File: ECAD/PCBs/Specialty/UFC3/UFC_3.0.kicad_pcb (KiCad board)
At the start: 2 copper layers, 101.6 x 53.3 mm, 13 parts, among them P1 Digital, P10 CONN_01X01, P11 CONN_01X01, P12 CONN_01X01, P13 CONN_01X01, P2 Power, P3 Analog, P4 Analog, P5 PWM, P6 PWM, P7 Communication, P8 CONN_01X01, P9 CONN_01X01

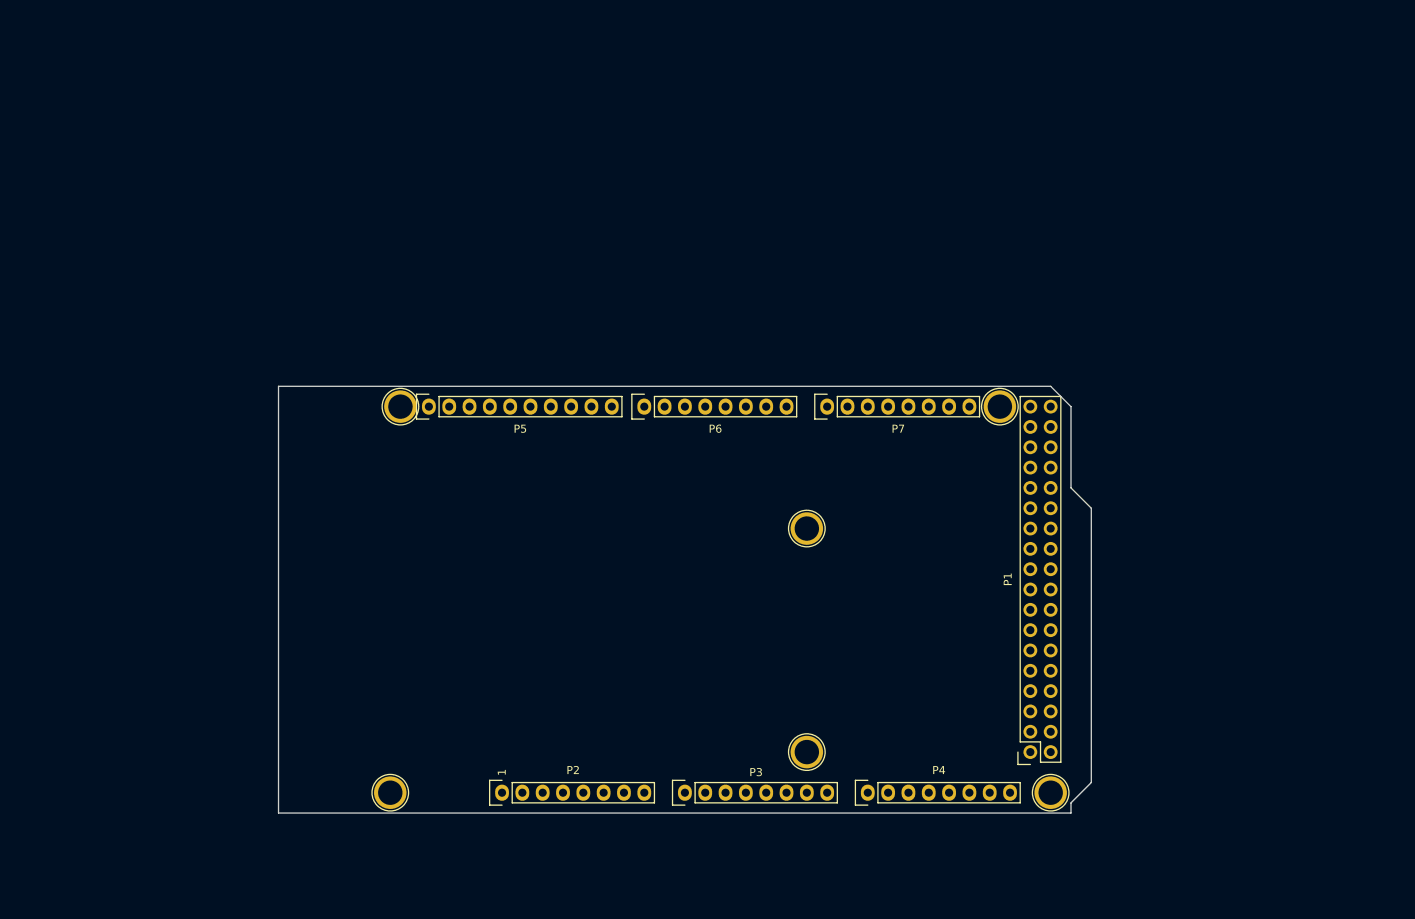
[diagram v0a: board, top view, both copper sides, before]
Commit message: temporary commit, this commit contains a partial version of the routing for UFC v3. along this commit I have added a python script to place the components based on the location listed on a csv file
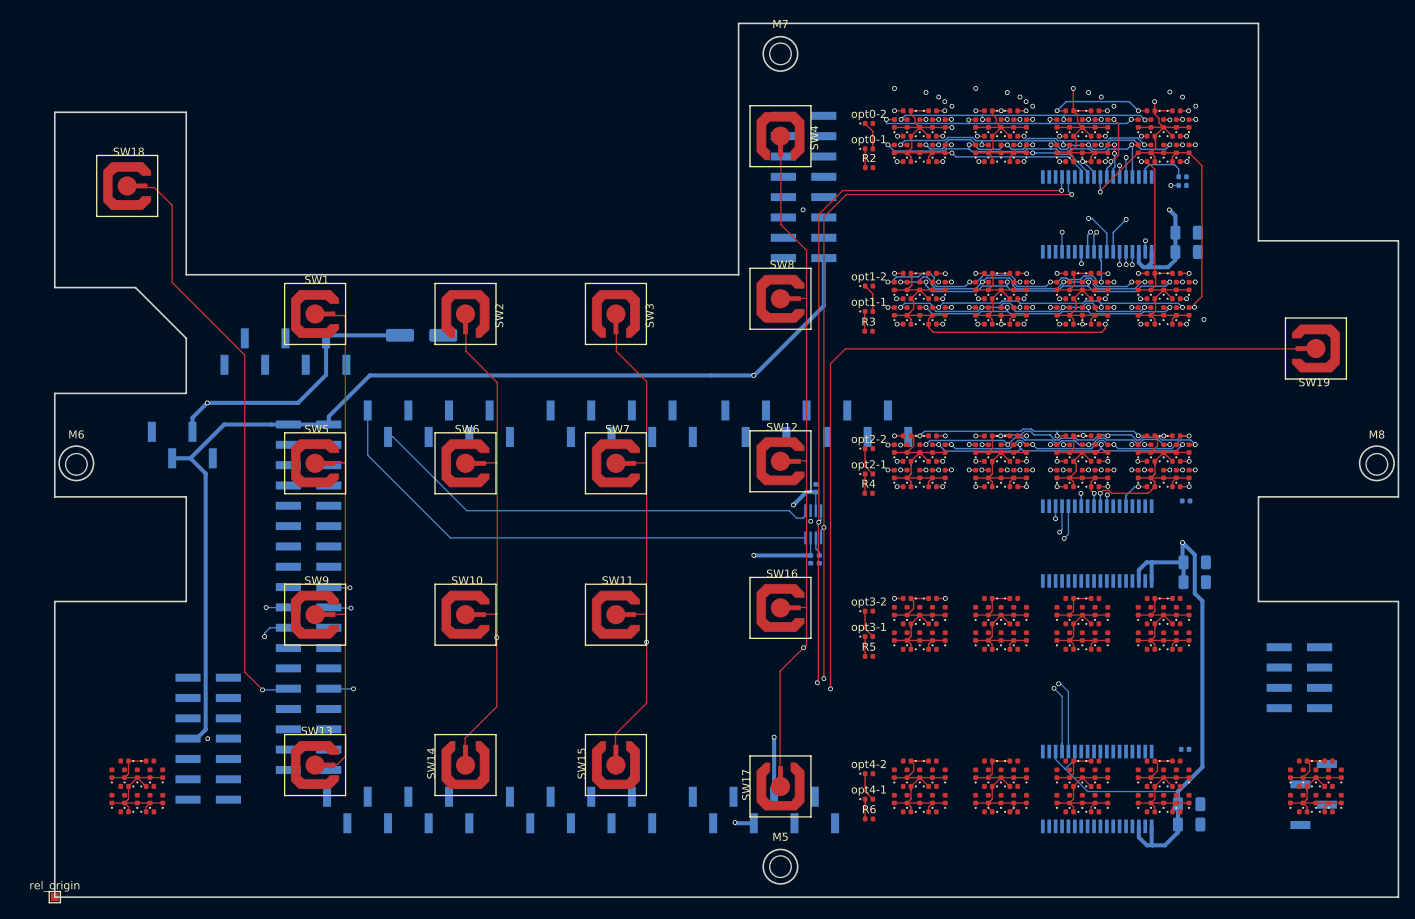
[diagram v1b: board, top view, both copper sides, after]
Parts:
- removed P1: Digital, Socket_Arduino_Mega:Socket_Strip_Arduino_2x18
- removed P2: Power, Socket_Arduino_Mega:Socket_Strip_Arduino_1x08
- removed P3, P4: Analog, Socket_Arduino_Mega:Socket_Strip_Arduino_1x08
- removed P5: PWM, Socket_Arduino_Mega:Socket_Strip_Arduino_1x10
- removed P6: PWM, Socket_Arduino_Mega:Socket_Strip_Arduino_1x08
- added C1: 47uF, Capacitor_SMD:C_1206_3216Metric, B.Cu at (216.9, 49.1)
- added C10: 100uF, Capacitor_SMD:C_1206_3216Metric, B.Cu at (217.2, 120.6)
- added C2: 100uF, Capacitor_SMD:C_1206_3216Metric, B.Cu at (216.9, 51.5)
- added C3: 22pF, Capacitor_SMD:C_0402_1005Metric, B.Cu at (216.4, 43.2)
- added C4: 1uF, Capacitor_SMD:C_0402_1005Metric, B.Cu at (170.5, 81.1)
- added C5: 1uF, Capacitor_SMD:C_0402_1005Metric, B.Cu at (169.9, 90.0)
- added C6: 47uF, Capacitor_SMD:C_1206_3216Metric, B.Cu at (217.9, 90.3)
- added C7: 100uF, Capacitor_SMD:C_1206_3216Metric, B.Cu at (217.9, 92.8)
- added C8: 220uF, Capacitor_SMD:CP_Elec_6.3x7.7, B.Cu at (121.3, 62.0)
- added C9: 47uF, Capacitor_SMD:C_1206_3216Metric, B.Cu at (217.2, 123.1)
- added D1: a, LED_SMD:LED_0402_1005Metric, F.Cu at (181.9, 33.9)
- added D10: g2, LED_SMD:LED_0402_1005Metric, F.Cu at (185.1, 37.1)
- added D100: c, LED_SMD:LED_0402_1005Metric, F.Cu at (217.2, 38.6)
- added D101: d1, LED_SMD:LED_0402_1005Metric, F.Cu at (215.6, 40.2)
- added D102: d2, LED_SMD:LED_0402_1005Metric, F.Cu at (212.4, 40.2)
- added D103: e, LED_SMD:LED_0402_1005Metric, F.Cu at (210.8, 38.6)
- added D104: f, LED_SMD:LED_0402_1005Metric, F.Cu at (210.8, 35.5)
- added D105: g1, LED_SMD:LED_0402_1005Metric, F.Cu at (212.4, 37.1)
- added D106: g2, LED_SMD:LED_0402_1005Metric, F.Cu at (215.6, 37.1)
- added D107: h, LED_SMD:LED_0402_1005Metric, F.Cu at (212.4, 35.5)
- added D108: i, LED_SMD:LED_0402_1005Metric, F.Cu at (214.0, 35.5)
- added D109: j, LED_SMD:LED_0402_1005Metric, F.Cu at (215.6, 35.5)
- added D11: h, LED_SMD:LED_0402_1005Metric, F.Cu at (181.9, 35.5)
- added D110: k, LED_SMD:LED_0402_1005Metric, F.Cu at (215.6, 38.6)
- added D111: L, LED_SMD:LED_0402_1005Metric, F.Cu at (214.0, 38.6)
- added D112: m, LED_SMD:LED_0402_1005Metric, F.Cu at (212.4, 38.6)
- added D113: a, LED_SMD:LED_0402_1005Metric, F.Cu at (212.4, 54.2)
- added D114: a2, LED_SMD:LED_0402_1005Metric, F.Cu at (215.6, 54.2)
- added D115: b, LED_SMD:LED_0402_1005Metric, F.Cu at (217.2, 55.8)
- added D116: c, LED_SMD:LED_0402_1005Metric, F.Cu at (217.2, 59.0)
- added D117: d1, LED_SMD:LED_0402_1005Metric, F.Cu at (215.6, 60.6)
- added D118: d2, LED_SMD:LED_0402_1005Metric, F.Cu at (212.4, 60.6)
- added D119: e, LED_SMD:LED_0402_1005Metric, F.Cu at (210.8, 59.0)
- added D12: i, LED_SMD:LED_0402_1005Metric, F.Cu at (183.5, 35.5)
- added D120: f, LED_SMD:LED_0402_1005Metric, F.Cu at (210.8, 55.8)
- added D121: g1, LED_SMD:LED_0402_1005Metric, F.Cu at (212.4, 57.4)
- added D122: g2, LED_SMD:LED_0402_1005Metric, F.Cu at (215.6, 57.4)
- added D123: h, LED_SMD:LED_0402_1005Metric, F.Cu at (212.4, 55.8)
- added D124: i, LED_SMD:LED_0402_1005Metric, F.Cu at (214.0, 55.8)
- added D125: j, LED_SMD:LED_0402_1005Metric, F.Cu at (215.6, 55.8)
- added D126: k, LED_SMD:LED_0402_1005Metric, F.Cu at (215.6, 59.0)
- added D127: L, LED_SMD:LED_0402_1005Metric, F.Cu at (214.0, 59.0)
- added D128: m, LED_SMD:LED_0402_1005Metric, F.Cu at (212.4, 59.0)
- added D129: a, LED_SMD:LED_0402_1005Metric, F.Cu at (181.9, 74.5)
- added D13: j, LED_SMD:LED_0402_1005Metric, F.Cu at (185.1, 35.5)
- added D130: a2, LED_SMD:LED_0402_1005Metric, F.Cu at (185.1, 74.5)
- added D131: b, LED_SMD:LED_0402_1005Metric, F.Cu at (186.7, 76.1)
- added D132: c, LED_SMD:LED_0402_1005Metric, F.Cu at (186.7, 79.3)
- added D133: d1, LED_SMD:LED_0402_1005Metric, F.Cu at (185.1, 80.9)
- added D134: d2, LED_SMD:LED_0402_1005Metric, F.Cu at (181.9, 80.9)
- added D135: e, LED_SMD:LED_0402_1005Metric, F.Cu at (180.4, 79.3)
- added D136: f, LED_SMD:LED_0402_1005Metric, F.Cu at (180.4, 76.1)
- added D137: g1, LED_SMD:LED_0402_1005Metric, F.Cu at (181.9, 77.7)
- added D138: g2, LED_SMD:LED_0402_1005Metric, F.Cu at (185.1, 77.7)
- added D139: h, LED_SMD:LED_0402_1005Metric, F.Cu at (181.9, 76.1)
- added D14: k, LED_SMD:LED_0402_1005Metric, F.Cu at (185.1, 38.6)
- added D140: i, LED_SMD:LED_0402_1005Metric, F.Cu at (183.5, 76.1)
- added D141: j, LED_SMD:LED_0402_1005Metric, F.Cu at (185.1, 76.1)
- added D142: k, LED_SMD:LED_0402_1005Metric, F.Cu at (185.1, 79.3)
- added D143: L, LED_SMD:LED_0402_1005Metric, F.Cu at (183.5, 79.3)
- added D144: m, LED_SMD:LED_0402_1005Metric, F.Cu at (181.9, 79.3)
- added D145: a, LED_SMD:LED_0402_1005Metric, F.Cu at (181.9, 94.8)
- added D146: a2, LED_SMD:LED_0402_1005Metric, F.Cu at (185.1, 94.8)
- added D147: b, LED_SMD:LED_0402_1005Metric, F.Cu at (186.7, 96.4)
- added D148: c, LED_SMD:LED_0402_1005Metric, F.Cu at (186.7, 99.6)
- added D149: d1, LED_SMD:LED_0402_1005Metric, F.Cu at (185.1, 101.2)
- added D15: L, LED_SMD:LED_0402_1005Metric, F.Cu at (183.5, 38.6)
- added D150: d2, LED_SMD:LED_0402_1005Metric, F.Cu at (181.9, 101.2)
- added D151: e, LED_SMD:LED_0402_1005Metric, F.Cu at (180.4, 99.6)
- added D152: f, LED_SMD:LED_0402_1005Metric, F.Cu at (180.4, 96.4)
- added D153: g1, LED_SMD:LED_0402_1005Metric, F.Cu at (181.9, 98.0)
- added D154: g2, LED_SMD:LED_0402_1005Metric, F.Cu at (185.1, 98.0)
- added D155: h, LED_SMD:LED_0402_1005Metric, F.Cu at (181.9, 96.4)
- added D156: i, LED_SMD:LED_0402_1005Metric, F.Cu at (183.5, 96.4)
- added D157: j, LED_SMD:LED_0402_1005Metric, F.Cu at (185.1, 96.4)
- added D158: k, LED_SMD:LED_0402_1005Metric, F.Cu at (185.1, 99.6)
- added D159: L, LED_SMD:LED_0402_1005Metric, F.Cu at (183.5, 99.6)
- added D16: m, LED_SMD:LED_0402_1005Metric, F.Cu at (181.9, 38.6)
- added D160: m, LED_SMD:LED_0402_1005Metric, F.Cu at (181.9, 99.6)
- added D161: a, LED_SMD:LED_0402_1005Metric, F.Cu at (192.1, 74.5)
- added D162: a2, LED_SMD:LED_0402_1005Metric, F.Cu at (195.3, 74.5)
- added D163: b, LED_SMD:LED_0402_1005Metric, F.Cu at (196.9, 76.1)
- added D164: c, LED_SMD:LED_0402_1005Metric, F.Cu at (196.9, 79.3)
- added D165: d1, LED_SMD:LED_0402_1005Metric, F.Cu at (195.3, 80.9)
- added D166: d2, LED_SMD:LED_0402_1005Metric, F.Cu at (192.1, 80.9)
- added D167: e, LED_SMD:LED_0402_1005Metric, F.Cu at (190.5, 79.3)
- added D168: f, LED_SMD:LED_0402_1005Metric, F.Cu at (190.5, 76.1)
- added D169: g1, LED_SMD:LED_0402_1005Metric, F.Cu at (192.1, 77.7)
- added D17: a, LED_SMD:LED_0402_1005Metric, F.Cu at (181.9, 54.2)
- added D170: g2, LED_SMD:LED_0402_1005Metric, F.Cu at (195.3, 77.7)
- added D171: h, LED_SMD:LED_0402_1005Metric, F.Cu at (192.1, 76.1)
- added D172: i, LED_SMD:LED_0402_1005Metric, F.Cu at (193.7, 76.1)
- added D173: j, LED_SMD:LED_0402_1005Metric, F.Cu at (195.3, 76.1)
- added D174: k, LED_SMD:LED_0402_1005Metric, F.Cu at (195.3, 79.3)
- added D175: L, LED_SMD:LED_0402_1005Metric, F.Cu at (193.7, 79.3)
- added D176: m, LED_SMD:LED_0402_1005Metric, F.Cu at (192.1, 79.3)
- added D177: a, LED_SMD:LED_0402_1005Metric, F.Cu at (192.1, 94.8)
- added D178: a2, LED_SMD:LED_0402_1005Metric, F.Cu at (195.3, 94.8)
- added D179: b, LED_SMD:LED_0402_1005Metric, F.Cu at (196.9, 96.4)
- added D18: a2, LED_SMD:LED_0402_1005Metric, F.Cu at (185.1, 54.2)
- added D180: c, LED_SMD:LED_0402_1005Metric, F.Cu at (196.9, 99.6)
- added D181: d1, LED_SMD:LED_0402_1005Metric, F.Cu at (195.3, 101.2)
- added D182: d2, LED_SMD:LED_0402_1005Metric, F.Cu at (192.1, 101.2)
- added D183: e, LED_SMD:LED_0402_1005Metric, F.Cu at (190.5, 99.6)
- added D184: f, LED_SMD:LED_0402_1005Metric, F.Cu at (190.5, 96.4)
- added D185: g1, LED_SMD:LED_0402_1005Metric, F.Cu at (192.1, 98.0)
- added D186: g2, LED_SMD:LED_0402_1005Metric, F.Cu at (195.3, 98.0)
- added D187: h, LED_SMD:LED_0402_1005Metric, F.Cu at (192.1, 96.4)
- added D188: i, LED_SMD:LED_0402_1005Metric, F.Cu at (193.7, 96.4)
- added D189: j, LED_SMD:LED_0402_1005Metric, F.Cu at (195.3, 96.4)
- added D19: b, LED_SMD:LED_0402_1005Metric, F.Cu at (186.7, 55.8)
- added D190: k, LED_SMD:LED_0402_1005Metric, F.Cu at (195.3, 99.6)
- added D191: L, LED_SMD:LED_0402_1005Metric, F.Cu at (193.7, 99.6)
- added D192: m, LED_SMD:LED_0402_1005Metric, F.Cu at (192.1, 99.6)
- added D193: a, LED_SMD:LED_0402_1005Metric, F.Cu at (202.3, 74.5)
- added D194: a2, LED_SMD:LED_0402_1005Metric, F.Cu at (205.4, 74.5)
- added D195: b, LED_SMD:LED_0402_1005Metric, F.Cu at (207.0, 76.1)
- added D196: c, LED_SMD:LED_0402_1005Metric, F.Cu at (207.0, 79.3)
- added D197: d1, LED_SMD:LED_0402_1005Metric, F.Cu at (205.4, 80.9)
- added D198: d2, LED_SMD:LED_0402_1005Metric, F.Cu at (202.3, 80.9)
- added D199: e, LED_SMD:LED_0402_1005Metric, F.Cu at (200.7, 79.3)
- added D2: a2, LED_SMD:LED_0402_1005Metric, F.Cu at (185.1, 33.9)
- added D20: c, LED_SMD:LED_0402_1005Metric, F.Cu at (186.7, 59.0)
- added D200: f, LED_SMD:LED_0402_1005Metric, F.Cu at (200.7, 76.1)
- added D201: g1, LED_SMD:LED_0402_1005Metric, F.Cu at (202.3, 77.7)
- added D202: g2, LED_SMD:LED_0402_1005Metric, F.Cu at (205.4, 77.7)
- added D203: h, LED_SMD:LED_0402_1005Metric, F.Cu at (202.3, 76.1)
- added D204: i, LED_SMD:LED_0402_1005Metric, F.Cu at (203.9, 76.1)
- added D205: j, LED_SMD:LED_0402_1005Metric, F.Cu at (205.4, 76.1)
- added D206: k, LED_SMD:LED_0402_1005Metric, F.Cu at (205.4, 79.3)
- added D207: L, LED_SMD:LED_0402_1005Metric, F.Cu at (203.9, 79.3)
- added D208: m, LED_SMD:LED_0402_1005Metric, F.Cu at (202.3, 79.3)
- added D209: a, LED_SMD:LED_0402_1005Metric, F.Cu at (202.3, 94.8)
- added D21: d1, LED_SMD:LED_0402_1005Metric, F.Cu at (185.1, 60.6)
- added D210: a2, LED_SMD:LED_0402_1005Metric, F.Cu at (205.4, 94.8)
- added D211: b, LED_SMD:LED_0402_1005Metric, F.Cu at (207.0, 96.4)
- added D212: c, LED_SMD:LED_0402_1005Metric, F.Cu at (207.0, 99.6)
- added D213: d1, LED_SMD:LED_0402_1005Metric, F.Cu at (205.4, 101.2)
- added D214: d2, LED_SMD:LED_0402_1005Metric, F.Cu at (202.3, 101.2)
- added D215: e, LED_SMD:LED_0402_1005Metric, F.Cu at (200.7, 99.6)
- added D216: f, LED_SMD:LED_0402_1005Metric, F.Cu at (200.7, 96.4)
- added D217: g1, LED_SMD:LED_0402_1005Metric, F.Cu at (202.3, 98.0)
- added D218: g2, LED_SMD:LED_0402_1005Metric, F.Cu at (205.4, 98.0)
- added D219: h, LED_SMD:LED_0402_1005Metric, F.Cu at (202.3, 96.4)
- added D22: d2, LED_SMD:LED_0402_1005Metric, F.Cu at (181.9, 60.6)
- added D220: i, LED_SMD:LED_0402_1005Metric, F.Cu at (203.9, 96.4)
- added D221: j, LED_SMD:LED_0402_1005Metric, F.Cu at (205.4, 96.4)
- added D222: k, LED_SMD:LED_0402_1005Metric, F.Cu at (205.4, 99.6)
- added D223: L, LED_SMD:LED_0402_1005Metric, F.Cu at (203.9, 99.6)
- added D224: m, LED_SMD:LED_0402_1005Metric, F.Cu at (202.3, 99.6)
- added D225: a, LED_SMD:LED_0402_1005Metric, F.Cu at (212.4, 74.5)
- added D226: a2, LED_SMD:LED_0402_1005Metric, F.Cu at (215.6, 74.5)
- added D227: b, LED_SMD:LED_0402_1005Metric, F.Cu at (217.2, 76.1)
- added D228: c, LED_SMD:LED_0402_1005Metric, F.Cu at (217.2, 79.3)
- added D229: d1, LED_SMD:LED_0402_1005Metric, F.Cu at (215.6, 80.9)
- added D23: e, LED_SMD:LED_0402_1005Metric, F.Cu at (180.4, 59.0)
- added D230: d2, LED_SMD:LED_0402_1005Metric, F.Cu at (212.4, 80.9)
- added D231: e, LED_SMD:LED_0402_1005Metric, F.Cu at (210.8, 79.3)
- added D232: f, LED_SMD:LED_0402_1005Metric, F.Cu at (210.8, 76.1)
- added D233: g1, LED_SMD:LED_0402_1005Metric, F.Cu at (212.4, 77.7)
- added D234: g2, LED_SMD:LED_0402_1005Metric, F.Cu at (215.6, 77.7)
- added D235: h, LED_SMD:LED_0402_1005Metric, F.Cu at (212.4, 76.1)
- added D236: i, LED_SMD:LED_0402_1005Metric, F.Cu at (214.0, 76.1)
- added D237: j, LED_SMD:LED_0402_1005Metric, F.Cu at (215.6, 76.1)
- added D238: k, LED_SMD:LED_0402_1005Metric, F.Cu at (215.6, 79.3)
- added D239: L, LED_SMD:LED_0402_1005Metric, F.Cu at (214.0, 79.3)
- added D24: f, LED_SMD:LED_0402_1005Metric, F.Cu at (180.4, 55.8)
- added D240: m, LED_SMD:LED_0402_1005Metric, F.Cu at (212.4, 79.3)
- added D241: a, LED_SMD:LED_0402_1005Metric, F.Cu at (212.4, 94.8)
- added D242: a2, LED_SMD:LED_0402_1005Metric, F.Cu at (215.6, 94.8)
- added D243: b, LED_SMD:LED_0402_1005Metric, F.Cu at (217.2, 96.4)
- added D244: c, LED_SMD:LED_0402_1005Metric, F.Cu at (217.2, 99.6)
- added D245: d1, LED_SMD:LED_0402_1005Metric, F.Cu at (215.6, 101.2)
- added D246: d2, LED_SMD:LED_0402_1005Metric, F.Cu at (212.4, 101.2)
- added D247: e, LED_SMD:LED_0402_1005Metric, F.Cu at (210.8, 99.6)
- added D248: f, LED_SMD:LED_0402_1005Metric, F.Cu at (210.8, 96.4)
- added D249: g1, LED_SMD:LED_0402_1005Metric, F.Cu at (212.4, 98.0)
- added D25: g1, LED_SMD:LED_0402_1005Metric, F.Cu at (181.9, 57.4)
- added D250: g2, LED_SMD:LED_0402_1005Metric, F.Cu at (215.6, 98.0)
- added D251: h, LED_SMD:LED_0402_1005Metric, F.Cu at (212.4, 96.4)
- added D252: i, LED_SMD:LED_0402_1005Metric, F.Cu at (214.0, 96.4)
- added D253: j, LED_SMD:LED_0402_1005Metric, F.Cu at (215.6, 96.4)
- added D254: k, LED_SMD:LED_0402_1005Metric, F.Cu at (215.6, 99.6)
- added D255: L, LED_SMD:LED_0402_1005Metric, F.Cu at (214.0, 99.6)
- added D256: m, LED_SMD:LED_0402_1005Metric, F.Cu at (212.4, 99.6)
- added D257: a, LED_SMD:LED_0402_1005Metric, F.Cu at (181.9, 115.2)
- added D258: a2, LED_SMD:LED_0402_1005Metric, F.Cu at (185.1, 115.2)
- added D259: b, LED_SMD:LED_0402_1005Metric, F.Cu at (186.7, 116.8)
- added D26: g2, LED_SMD:LED_0402_1005Metric, F.Cu at (185.1, 57.4)
- added D260: c, LED_SMD:LED_0402_1005Metric, F.Cu at (186.7, 119.9)
- added D261: d1, LED_SMD:LED_0402_1005Metric, F.Cu at (185.1, 121.5)
- added D262: d2, LED_SMD:LED_0402_1005Metric, F.Cu at (181.9, 121.5)
- added D263: e, LED_SMD:LED_0402_1005Metric, F.Cu at (180.4, 119.9)
- added D264: f, LED_SMD:LED_0402_1005Metric, F.Cu at (180.4, 116.8)
- added D265: g1, LED_SMD:LED_0402_1005Metric, F.Cu at (181.9, 118.3)
- added D266: g2, LED_SMD:LED_0402_1005Metric, F.Cu at (185.1, 118.3)
- added D267: h, LED_SMD:LED_0402_1005Metric, F.Cu at (181.9, 116.8)
- added D268: i, LED_SMD:LED_0402_1005Metric, F.Cu at (183.5, 116.8)
- added D269: j, LED_SMD:LED_0402_1005Metric, F.Cu at (185.1, 116.8)
- added D27: h, LED_SMD:LED_0402_1005Metric, F.Cu at (181.9, 55.8)
- added D270: k, LED_SMD:LED_0402_1005Metric, F.Cu at (185.1, 119.9)
- added D271: L, LED_SMD:LED_0402_1005Metric, F.Cu at (183.5, 119.9)
- added D272: m, LED_SMD:LED_0402_1005Metric, F.Cu at (181.9, 119.9)
- added D273: a, LED_SMD:LED_0402_1005Metric, F.Cu at (84.1, 115.2)
- added D274: a2, LED_SMD:LED_0402_1005Metric, F.Cu at (87.3, 115.2)
- added D275: b, LED_SMD:LED_0402_1005Metric, F.Cu at (88.9, 116.8)
- added D276: c, LED_SMD:LED_0402_1005Metric, F.Cu at (88.9, 119.9)
- added D277: d1, LED_SMD:LED_0402_1005Metric, F.Cu at (87.3, 121.5)
- added D278: d2, LED_SMD:LED_0402_1005Metric, F.Cu at (84.1, 121.5)
- added D279: e, LED_SMD:LED_0402_1005Metric, F.Cu at (82.5, 119.9)
- added D28: i, LED_SMD:LED_0402_1005Metric, F.Cu at (183.5, 55.8)
- added D280: f, LED_SMD:LED_0402_1005Metric, F.Cu at (82.5, 116.8)
- added D281: g1, LED_SMD:LED_0402_1005Metric, F.Cu at (84.1, 118.3)
- added D282: g2, LED_SMD:LED_0402_1005Metric, F.Cu at (87.3, 118.3)
- added D283: h, LED_SMD:LED_0402_1005Metric, F.Cu at (84.1, 116.8)
- added D284: i, LED_SMD:LED_0402_1005Metric, F.Cu at (85.7, 116.8)
- added D285: j, LED_SMD:LED_0402_1005Metric, F.Cu at (87.3, 116.8)
- added D286: k, LED_SMD:LED_0402_1005Metric, F.Cu at (87.3, 119.9)
- added D287: L, LED_SMD:LED_0402_1005Metric, F.Cu at (85.7, 119.9)
- added D288: m, LED_SMD:LED_0402_1005Metric, F.Cu at (84.1, 119.9)
- added D289: a, LED_SMD:LED_0402_1005Metric, F.Cu at (192.1, 115.2)
- added D29: j, LED_SMD:LED_0402_1005Metric, F.Cu at (185.1, 55.8)
- added D290: a2, LED_SMD:LED_0402_1005Metric, F.Cu at (195.3, 115.2)
- added D291: b, LED_SMD:LED_0402_1005Metric, F.Cu at (196.9, 116.8)
- added D292: c, LED_SMD:LED_0402_1005Metric, F.Cu at (196.9, 119.9)
- added D293: d1, LED_SMD:LED_0402_1005Metric, F.Cu at (195.3, 121.5)
- added D294: d2, LED_SMD:LED_0402_1005Metric, F.Cu at (192.1, 121.5)
- added D295: e, LED_SMD:LED_0402_1005Metric, F.Cu at (190.5, 119.9)
- added D296: f, LED_SMD:LED_0402_1005Metric, F.Cu at (190.5, 116.8)
- added D297: g1, LED_SMD:LED_0402_1005Metric, F.Cu at (192.1, 118.3)
- added D298: g2, LED_SMD:LED_0402_1005Metric, F.Cu at (195.3, 118.3)
- added D299: h, LED_SMD:LED_0402_1005Metric, F.Cu at (192.1, 116.8)
- added D3: b, LED_SMD:LED_0402_1005Metric, F.Cu at (186.7, 35.5)
- added D30: k, LED_SMD:LED_0402_1005Metric, F.Cu at (185.1, 59.0)
- added D300: i, LED_SMD:LED_0402_1005Metric, F.Cu at (193.7, 116.8)
- added D301: j, LED_SMD:LED_0402_1005Metric, F.Cu at (195.3, 116.8)
- added D302: k, LED_SMD:LED_0402_1005Metric, F.Cu at (195.3, 119.9)
- added D303: L, LED_SMD:LED_0402_1005Metric, F.Cu at (193.7, 119.9)
- added D304: m, LED_SMD:LED_0402_1005Metric, F.Cu at (192.1, 119.9)
- added D305: a, LED_SMD:LED_0402_1005Metric, F.Cu at (231.5, 115.2)
- added D306: a2, LED_SMD:LED_0402_1005Metric, F.Cu at (234.6, 115.2)
- added D307: b, LED_SMD:LED_0402_1005Metric, F.Cu at (236.2, 116.8)
- added D308: c, LED_SMD:LED_0402_1005Metric, F.Cu at (236.2, 119.9)
- added D309: d1, LED_SMD:LED_0402_1005Metric, F.Cu at (234.6, 121.5)
- added D31: L, LED_SMD:LED_0402_1005Metric, F.Cu at (183.5, 59.0)
- added D310: d2, LED_SMD:LED_0402_1005Metric, F.Cu at (231.5, 121.5)
- added D311: e, LED_SMD:LED_0402_1005Metric, F.Cu at (229.9, 119.9)
- added D312: f, LED_SMD:LED_0402_1005Metric, F.Cu at (229.9, 116.8)
- added D313: g1, LED_SMD:LED_0402_1005Metric, F.Cu at (231.5, 118.3)
- added D314: g2, LED_SMD:LED_0402_1005Metric, F.Cu at (234.6, 118.3)
- added D315: h, LED_SMD:LED_0402_1005Metric, F.Cu at (231.5, 116.8)
- added D316: i, LED_SMD:LED_0402_1005Metric, F.Cu at (233.0, 116.8)
- added D317: j, LED_SMD:LED_0402_1005Metric, F.Cu at (234.6, 116.8)
- added D318: k, LED_SMD:LED_0402_1005Metric, F.Cu at (234.6, 119.9)
- added D319: L, LED_SMD:LED_0402_1005Metric, F.Cu at (233.0, 119.9)
- added D32: m, LED_SMD:LED_0402_1005Metric, F.Cu at (181.9, 59.0)
- added D320: m, LED_SMD:LED_0402_1005Metric, F.Cu at (231.5, 119.9)
- added D321: a, LED_SMD:LED_0402_1005Metric, F.Cu at (202.3, 115.2)
- added D322: a2, LED_SMD:LED_0402_1005Metric, F.Cu at (205.4, 115.2)
- added D323: b, LED_SMD:LED_0402_1005Metric, F.Cu at (207.0, 116.8)
- added D324: c, LED_SMD:LED_0402_1005Metric, F.Cu at (207.0, 119.9)
- added D325: d1, LED_SMD:LED_0402_1005Metric, F.Cu at (205.4, 121.5)
- added D326: d2, LED_SMD:LED_0402_1005Metric, F.Cu at (202.3, 121.5)
- added D327: e, LED_SMD:LED_0402_1005Metric, F.Cu at (200.7, 119.9)
- added D328: f, LED_SMD:LED_0402_1005Metric, F.Cu at (200.7, 116.8)
- added D329: g1, LED_SMD:LED_0402_1005Metric, F.Cu at (202.3, 118.3)
- added D33: a, LED_SMD:LED_0402_1005Metric, F.Cu at (192.1, 33.9)
- added D330: g2, LED_SMD:LED_0402_1005Metric, F.Cu at (205.4, 118.3)
- added D331: h, LED_SMD:LED_0402_1005Metric, F.Cu at (202.3, 116.8)
- added D332: i, LED_SMD:LED_0402_1005Metric, F.Cu at (203.9, 116.8)
- added D333: j, LED_SMD:LED_0402_1005Metric, F.Cu at (205.4, 116.8)
- added D334: k, LED_SMD:LED_0402_1005Metric, F.Cu at (205.4, 119.9)
- added D335: L, LED_SMD:LED_0402_1005Metric, F.Cu at (203.9, 119.9)
- added D336: m, LED_SMD:LED_0402_1005Metric, F.Cu at (202.3, 119.9)
- added D337: a, LED_SMD:LED_0402_1005Metric, F.Cu at (212.4, 115.2)
- added D338: a2, LED_SMD:LED_0402_1005Metric, F.Cu at (215.6, 115.2)
- added D339: b, LED_SMD:LED_0402_1005Metric, F.Cu at (217.2, 116.8)
- added D34: a2, LED_SMD:LED_0402_1005Metric, F.Cu at (195.3, 33.9)
- added D340: c, LED_SMD:LED_0402_1005Metric, F.Cu at (217.2, 119.9)
- added D341: d1, LED_SMD:LED_0402_1005Metric, F.Cu at (215.6, 121.5)
- added D342: d2, LED_SMD:LED_0402_1005Metric, F.Cu at (212.4, 121.5)
- added D343: e, LED_SMD:LED_0402_1005Metric, F.Cu at (210.8, 119.9)
- added D344: f, LED_SMD:LED_0402_1005Metric, F.Cu at (210.8, 116.8)
- added D345: g1, LED_SMD:LED_0402_1005Metric, F.Cu at (212.4, 118.3)
- added D346: g2, LED_SMD:LED_0402_1005Metric, F.Cu at (215.6, 118.3)
- added D347: h, LED_SMD:LED_0402_1005Metric, F.Cu at (212.4, 116.8)
- added D348: i, LED_SMD:LED_0402_1005Metric, F.Cu at (214.0, 116.8)
- added D349: j, LED_SMD:LED_0402_1005Metric, F.Cu at (215.6, 116.8)
- added D35: b, LED_SMD:LED_0402_1005Metric, F.Cu at (196.9, 35.5)
- added D350: k, LED_SMD:LED_0402_1005Metric, F.Cu at (215.6, 119.9)
- added D351: L, LED_SMD:LED_0402_1005Metric, F.Cu at (214.0, 119.9)
- added D352: m, LED_SMD:LED_0402_1005Metric, F.Cu at (212.4, 119.9)
- added D36: c, LED_SMD:LED_0402_1005Metric, F.Cu at (196.9, 38.6)
- added D37: d1, LED_SMD:LED_0402_1005Metric, F.Cu at (195.3, 40.2)
- added D38: d2, LED_SMD:LED_0402_1005Metric, F.Cu at (192.1, 40.2)
- added D39: e, LED_SMD:LED_0402_1005Metric, F.Cu at (190.5, 38.6)
- added D4: c, LED_SMD:LED_0402_1005Metric, F.Cu at (186.7, 38.6)
- added D40: f, LED_SMD:LED_0402_1005Metric, F.Cu at (190.5, 35.5)
- added D41: g1, LED_SMD:LED_0402_1005Metric, F.Cu at (192.1, 37.1)
- added D42: g2, LED_SMD:LED_0402_1005Metric, F.Cu at (195.3, 37.1)
- added D43: h, LED_SMD:LED_0402_1005Metric, F.Cu at (192.1, 35.5)
- added D44: i, LED_SMD:LED_0402_1005Metric, F.Cu at (193.7, 35.5)
- added D45: j, LED_SMD:LED_0402_1005Metric, F.Cu at (195.3, 35.5)
- added D46: k, LED_SMD:LED_0402_1005Metric, F.Cu at (195.3, 38.6)
- added D47: L, LED_SMD:LED_0402_1005Metric, F.Cu at (193.7, 38.6)
- added D48: m, LED_SMD:LED_0402_1005Metric, F.Cu at (192.1, 38.6)
- added D49: a, LED_SMD:LED_0402_1005Metric, F.Cu at (192.1, 54.2)
- added D5: d1, LED_SMD:LED_0402_1005Metric, F.Cu at (185.1, 40.2)
- added D50: a2, LED_SMD:LED_0402_1005Metric, F.Cu at (195.3, 54.2)
- added D51: b, LED_SMD:LED_0402_1005Metric, F.Cu at (196.9, 55.8)
- added D52: c, LED_SMD:LED_0402_1005Metric, F.Cu at (196.9, 59.0)
- added D53: d1, LED_SMD:LED_0402_1005Metric, F.Cu at (195.3, 60.6)
- added D54: d2, LED_SMD:LED_0402_1005Metric, F.Cu at (192.1, 60.6)
- added D55: e, LED_SMD:LED_0402_1005Metric, F.Cu at (190.5, 59.0)
- added D56: f, LED_SMD:LED_0402_1005Metric, F.Cu at (190.5, 55.8)
- added D57: g1, LED_SMD:LED_0402_1005Metric, F.Cu at (192.1, 57.4)
- added D58: g2, LED_SMD:LED_0402_1005Metric, F.Cu at (195.3, 57.4)
- added D59: h, LED_SMD:LED_0402_1005Metric, F.Cu at (192.1, 55.8)
- added D6: d2, LED_SMD:LED_0402_1005Metric, F.Cu at (181.9, 40.2)
- added D60: i, LED_SMD:LED_0402_1005Metric, F.Cu at (193.7, 55.8)
- added D61: j, LED_SMD:LED_0402_1005Metric, F.Cu at (195.3, 55.8)
- added D62: k, LED_SMD:LED_0402_1005Metric, F.Cu at (195.3, 59.0)
- added D63: L, LED_SMD:LED_0402_1005Metric, F.Cu at (193.7, 59.0)
- added D64: m, LED_SMD:LED_0402_1005Metric, F.Cu at (192.1, 59.0)
- added D65: a, LED_SMD:LED_0402_1005Metric, F.Cu at (202.3, 33.9)
- added D66: a2, LED_SMD:LED_0402_1005Metric, F.Cu at (205.4, 33.9)
- added D67: b, LED_SMD:LED_0402_1005Metric, F.Cu at (207.0, 35.5)
- added D68: c, LED_SMD:LED_0402_1005Metric, F.Cu at (207.0, 38.6)
- added D69: d1, LED_SMD:LED_0402_1005Metric, F.Cu at (205.4, 40.2)
- added D7: e, LED_SMD:LED_0402_1005Metric, F.Cu at (180.4, 38.6)
- added D70: d2, LED_SMD:LED_0402_1005Metric, F.Cu at (202.3, 40.2)
- added D71: e, LED_SMD:LED_0402_1005Metric, F.Cu at (200.7, 38.6)
- added D72: f, LED_SMD:LED_0402_1005Metric, F.Cu at (200.7, 35.5)
- added D73: g1, LED_SMD:LED_0402_1005Metric, F.Cu at (202.3, 37.1)
- added D74: g2, LED_SMD:LED_0402_1005Metric, F.Cu at (205.4, 37.1)
- added D75: h, LED_SMD:LED_0402_1005Metric, F.Cu at (202.3, 35.5)
- added D76: i, LED_SMD:LED_0402_1005Metric, F.Cu at (203.9, 35.5)
- added D77: j, LED_SMD:LED_0402_1005Metric, F.Cu at (205.4, 35.5)
- added D78: k, LED_SMD:LED_0402_1005Metric, F.Cu at (205.4, 38.6)
- added D79: L, LED_SMD:LED_0402_1005Metric, F.Cu at (203.9, 38.6)
- added D8: f, LED_SMD:LED_0402_1005Metric, F.Cu at (180.4, 35.5)
- added D80: m, LED_SMD:LED_0402_1005Metric, F.Cu at (202.3, 38.6)
- added D81: a, LED_SMD:LED_0402_1005Metric, F.Cu at (202.3, 54.2)
- added D82: a2, LED_SMD:LED_0402_1005Metric, F.Cu at (205.4, 54.2)
- added D83: b, LED_SMD:LED_0402_1005Metric, F.Cu at (207.0, 55.8)
- added D84: c, LED_SMD:LED_0402_1005Metric, F.Cu at (207.0, 59.0)
- added D85: d1, LED_SMD:LED_0402_1005Metric, F.Cu at (205.4, 60.6)
- added D86: d2, LED_SMD:LED_0402_1005Metric, F.Cu at (202.3, 60.6)
- added D87: e, LED_SMD:LED_0402_1005Metric, F.Cu at (200.7, 59.0)
- added D88: f, LED_SMD:LED_0402_1005Metric, F.Cu at (200.7, 55.8)
- added D89: g1, LED_SMD:LED_0402_1005Metric, F.Cu at (202.3, 57.4)
- added D9: g1, LED_SMD:LED_0402_1005Metric, F.Cu at (181.9, 37.1)
- added D90: g2, LED_SMD:LED_0402_1005Metric, F.Cu at (205.4, 57.4)
- added D91: h, LED_SMD:LED_0402_1005Metric, F.Cu at (202.3, 55.8)
- added D92: i, LED_SMD:LED_0402_1005Metric, F.Cu at (203.9, 55.8)
- added D93: j, LED_SMD:LED_0402_1005Metric, F.Cu at (205.4, 55.8)
- added D94: k, LED_SMD:LED_0402_1005Metric, F.Cu at (205.4, 59.0)
- added D95: L, LED_SMD:LED_0402_1005Metric, F.Cu at (203.9, 59.0)
- added D96: m, LED_SMD:LED_0402_1005Metric, F.Cu at (202.3, 59.0)
- added D97: a, LED_SMD:LED_0402_1005Metric, F.Cu at (212.4, 33.9)
- added D98: a2, LED_SMD:LED_0402_1005Metric, F.Cu at (215.6, 33.9)
- added D99: b, LED_SMD:LED_0402_1005Metric, F.Cu at (217.2, 35.5)
- added J1: PWR IN, Connector_PinHeader_2.54mm:PinHeader_1x04_P2.54mm_Vertical_SMD_Pin1Left, B.Cu at (91.4, 75.7)
- added J2: OLED DISP, Connector_PinHeader_2.54mm:PinHeader_1x07_P2.54mm_Vertical_SMD_Pin1Left, B.Cu at (104.2, 64.0)
- added J3: PANEL SW, Connector_PinHeader_2.54mm:PinHeader_2x07_P2.54mm_Vertical_SMD, B.Cu at (94.6, 112.4)
- added J4: HUD BIT, Connector_PinHeader_2.54mm:PinHeader_1x04_P2.54mm_Vertical_SMD_Pin1Left, B.Cu at (232.8, 119.4)
- added J5: AP BTNS, Connector_PinHeader_2.54mm:PinHeader_2x04_P2.54mm_Vertical_SMD, B.Cu at (231.0, 104.7)
- added J6: HUD PANL, Connector_PinHeader_2.54mm:PinHeader_2x08_P2.54mm_Vertical_SMD, B.Cu at (169.0, 43.4)
- added M5: mounting hole, MountingHole:MountingHole_2.7mm_M2.5, F.Cu at (166.1, 128.4)
- added M6: mounting hole, MountingHole:MountingHole_2.7mm_M2.5, F.Cu at (78.1, 78.1)
- added M7: mounting hole, MountingHole:MountingHole_2.7mm_M2.5, F.Cu at (166.1, 26.8)
- added M8: mounting hole, MountingHole:MountingHole_2.7mm_M2.5, F.Cu at (240.7, 78.1)
- added R1: 56k, Resistor_SMD:R_0402_1005Metric, B.Cu at (216.4, 42.1)
- added R2: 330, Resistor_SMD:R_0402_1005Metric, F.Cu at (177.2, 41.0)
- added R3: 330, Resistor_SMD:R_0402_1005Metric, F.Cu at (177.1, 61.4)
- added R4: 330, Resistor_SMD:R_0402_1005Metric, F.Cu at (177.1, 81.7)
- added R5: 330, Resistor_SMD:R_0402_1005Metric, F.Cu at (177.2, 102.1)
- added R6: 330, Resistor_SMD:R_0402_1005Metric, F.Cu at (177.2, 122.4)
- added R7: 56k, Resistor_SMD:R_0402_1005Metric, B.Cu at (216.8, 82.7)
- added R8: 56k, Resistor_SMD:R_0402_1005Metric, B.Cu at (216.7, 113.7)
- added R9: 56k, Resistor_SMD:R_0402_1005Metric, B.Cu at (171.0, 90.0)
- added SW1: 1, KiCAD Libraries:SWITCH_SNAP_DOME, F.Cu at (108.0, 59.3)
- added SW10: 8, KiCAD Libraries:SWITCH_SNAP_DOME, F.Cu at (126.8, 96.9)
- added SW11: 9, KiCAD Libraries:SWITCH_SNAP_DOME, F.Cu at (145.6, 96.9)
- added SW12: OPT3, KiCAD Libraries:SWITCH_SNAP_DOME, F.Cu at (166.1, 77.7)
- added SW13: CLR, KiCAD Libraries:SWITCH_SNAP_DOME, F.Cu at (108.0, 115.7)
- added SW14: ~0, KiCAD Libraries:SWITCH_SNAP_DOME, F.Cu at (126.8, 115.7)
- added SW15: ENT, KiCAD Libraries:SWITCH_SNAP_DOME, F.Cu at (145.6, 115.7)
- added SW16: OPT4, KiCAD Libraries:SWITCH_SNAP_DOME, F.Cu at (166.1, 96.0)
- added SW17: OPT5, KiCAD Libraries:SWITCH_SNAP_DOME, F.Cu at (166.1, 118.3)
- added SW18: I/P, KiCAD Libraries:SWITCH_SNAP_DOME, F.Cu at (84.5, 43.3)
- added SW19: EMCON, KiCAD Libraries:SWITCH_SNAP_DOME, F.Cu at (233.1, 63.6)
- added SW2: 2, KiCAD Libraries:SWITCH_SNAP_DOME, F.Cu at (126.8, 59.3)
- added SW3: 3, KiCAD Libraries:SWITCH_SNAP_DOME, F.Cu at (145.6, 59.3)
- added SW4: OPT1, KiCAD Libraries:SWITCH_SNAP_DOME, F.Cu at (166.1, 37.1)
- added SW5: 4, KiCAD Libraries:SWITCH_SNAP_DOME, F.Cu at (108.0, 78.0)
- added SW6: 5, KiCAD Libraries:SWITCH_SNAP_DOME, F.Cu at (126.8, 78.0)
- added SW7: 6, KiCAD Libraries:SWITCH_SNAP_DOME, F.Cu at (145.6, 78.0)
- added SW8: OPT2, KiCAD Libraries:SWITCH_SNAP_DOME, F.Cu at (166.1, 57.4)
- added SW9: 7, KiCAD Libraries:SWITCH_SNAP_DOME, F.Cu at (108.0, 96.9)
- added U1: MAX6955AAX+, KiCAD Libraries:SSOP-36, B.Cu at (205.7, 46.8)
- added U2: TXS0102DCT, Package_SO:SSOP-8_2.95x2.8mm_P0.65mm, B.Cu at (170.2, 85.6)
- added U3: MAX6955AAX+, KiCAD Libraries:SSOP-36, B.Cu at (205.7, 88.0)
- added U4: MAX6955AAX+, KiCAD Libraries:SSOP-36, B.Cu at (205.7, 118.7)
- added opt0-1: OPT 0,0, LED_SMD:LED_0402_1005Metric, F.Cu at (177.2, 38.6)
- added opt0-2: OPT 0,1, LED_SMD:LED_0402_1005Metric, F.Cu at (177.2, 35.5)
- added opt1-1: OPT 1,0, LED_SMD:LED_0402_1005Metric, F.Cu at (177.2, 59.0)
- added opt1-2: OPT 1,1, LED_SMD:LED_0402_1005Metric, F.Cu at (177.2, 55.8)
- added opt2-1: OPT 2,0, LED_SMD:LED_0402_1005Metric, F.Cu at (177.2, 79.3)
- added opt2-2: OPT 2,1, LED_SMD:LED_0402_1005Metric, F.Cu at (177.2, 76.1)
- added opt3-1: OPT 3,0, LED_SMD:LED_0402_1005Metric, F.Cu at (177.2, 99.6)
- added opt3-2: OPT 3,1, LED_SMD:LED_0402_1005Metric, F.Cu at (177.2, 96.4)
- added opt4-1: OPT 4,0, LED_SMD:LED_0402_1005Metric, F.Cu at (177.2, 119.9)
- added opt4-2: OPT 4,1, LED_SMD:LED_0402_1005Metric, F.Cu at (177.2, 116.8)
- added rel_origin: TestPoint_Pad_1.0x1.0mm, TestPoint:TestPoint_Pad_1.0x1.0mm, F.Cu at (75.4, 132.2)
- P10: value CONN_01X01 -> PWM; footprint Socket_Arduino_Mega:Arduino_1pin -> Connector_PinHeader_2.54mm:PinHeader_1x08_P2.54mm_Vertical_SMD_Pin1Left; moved to B.Cu
- P11, P9: value CONN_01X01 -> Analog; footprint Socket_Arduino_Mega:Arduino_1pin -> Connector_PinHeader_2.54mm:PinHeader_1x08_P2.54mm_Vertical_SMD_Pin1Left; moved to B.Cu
- P12: value CONN_01X01 -> Communication; footprint Socket_Arduino_Mega:Arduino_1pin -> Connector_PinHeader_2.54mm:PinHeader_1x08_P2.54mm_Vertical_SMD_Pin1Left; moved to B.Cu
- P13: value CONN_01X01 -> Digital; footprint Socket_Arduino_Mega:Arduino_1pin -> Connector_PinHeader_2.54mm:PinHeader_2x18_P2.54mm_Vertical_SMD; moved to B.Cu
- P7: value Communication -> PWM; footprint Socket_Arduino_Mega:Socket_Strip_Arduino_1x08 -> Connector_PinHeader_2.54mm:PinHeader_1x10_P2.54mm_Vertical_SMD_Pin1Left; moved to B.Cu
- P8: value CONN_01X01 -> Power; footprint Socket_Arduino_Mega:Arduino_1pin -> Connector_PinHeader_2.54mm:PinHeader_1x08_P2.54mm_Vertical_SMD_Pin1Left; moved to B.Cu
- moved P13 89.6 mm to (107.1, 94.7)
- moved P10 70.7 mm to (146.3, 73.0), turned to 90 degrees
- moved P11 50.4 mm to (118.3, 121.3), turned to 270 degrees
- moved P12 47.8 mm to (123.4, 73.0), turned to 90 degrees
- moved P8 46.8 mm to (164.1, 121.3), turned to 90 degrees
- moved P9 29.1 mm to (141.2, 121.3), turned to 90 degrees
- moved P7 2.50 mm to (170.7, 73.0), turned to 270 degrees
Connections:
- P10 pad 1: Net-(P10-Pad1) -> /7(**)
- P11 pad 1: Net-(P11-Pad1) -> /A8
- P12 pad 1: Net-(P12-Pad1) -> /14(Tx3)
- P13 pad 1: Net-(P13-Pad1) -> GND
- P7 pad 1: /14(Tx3) -> /SCL
- P7 pad 2: /15(Rx3) -> /SDA
- P7 pad 3: /16(Tx2) -> /AREF
- P7 pad 4: /17(Rx2) -> GND
- P7 pad 5: /18(Tx1) -> /13(**)
- P7 pad 6: /19(Rx1) -> /12(**)
- P7 pad 7: /20(SDA) -> /11(**)
- P7 pad 8: /21(SCL) -> /10(**)
- P9 pad 1: Net-(P9-Pad1) -> /A0
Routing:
- net +3V3: track 0.00 -> 424.9 mm, vias 0 -> 8
- net +5V: track 0.00 -> 201.9 mm, vias 0 -> 3
- net /SCL3v: track 0.00 -> 167.2 mm, vias 0 -> 5
- net /SDA3v: track 0.00 -> 165.7 mm, vias 0 -> 5
- net /47: track 0.00 -> 162.6 mm, vias 0 -> 2
- net /40: track 0.00 -> 154.3 mm, vias 0 -> 2
- net /O2-0: track 0.00 -> 143.0 mm, vias 0 -> 10
- net /O4-0: track 0.00 -> 138.8 mm, vias 0 -> 11
- net /O0-0: track 0.00 -> 126.4 mm, vias 0 -> 8
- net /O3-0: track 0.00 -> 122.2 mm, vias 0 -> 10
- net /O1-0: track 0.00 -> 119.3 mm, vias 0 -> 8
- net /O13-0: track 0.00 -> 118.7 mm, vias 0 -> 13
- net /O5-0: track 0.00 -> 117.3 mm, vias 0 -> 9
- net /O16-0: track 0.00 -> 108.0 mm, vias 0 -> 9
- net /O12-0: track 0.00 -> 107.6 mm, vias 0 -> 9
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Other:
- board size 101.6 x 53.3 mm -> 168 x 109.2 mm
- copper layers 2 -> 4
- net class Default: clearance 0.2 -> 0.1016; trace_width 0.25 -> 0.1778
- net class control added: clearance 0.1016, trace_width 0.127, via_dia 0.6, via_drill 0.4
- net class power added: clearance 0.1778, trace_width 0.508, via_dia 0.6, via_drill 0.4
- rule trace_clearance: 0.2 -> 0.1016
- rule trace_min: 0.2 -> 0.127
- board text added: "The arduino connector is designed for Arduino Mega to be connected on the Front of the arduino... this board assumes the connector is on the back. this requires the existing connectors to be removed and soldered on the other side of the board"
